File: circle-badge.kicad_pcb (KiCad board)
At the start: 2 copper layers, 100 x 140 mm, 41 parts, among them J3 USB_C_Receptacle_USB2.0_16P, J4 Qwiic, Q1 CJ2302, Q2 CJ2305, SW1 POWER, SW4 RESET, SW5 SELECT, U1 HX9193-33GB, U2 QX2304, U3 Wio-SX1262, U4 ESP32-C3-MINI-1, X1 #badgelife

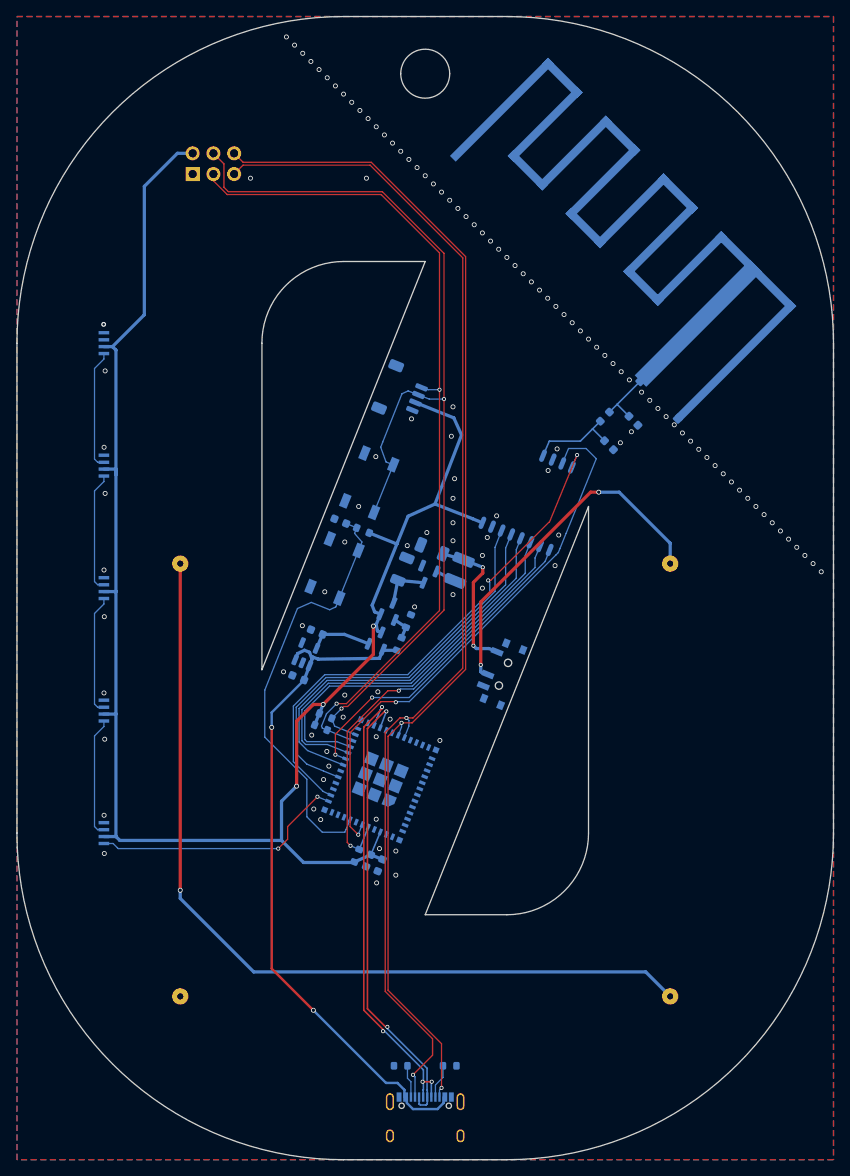
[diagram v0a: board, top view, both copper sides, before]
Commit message: Added front artwork and token on the back
Also:
- Tweaked the trace to the antenna to hopefully better match 50ohm impedance
- Tweaked all traces to use fillet on all corners
- Added/fixed parts information

Signed-off-by: Thomas Flummer <tf@flummer.net>
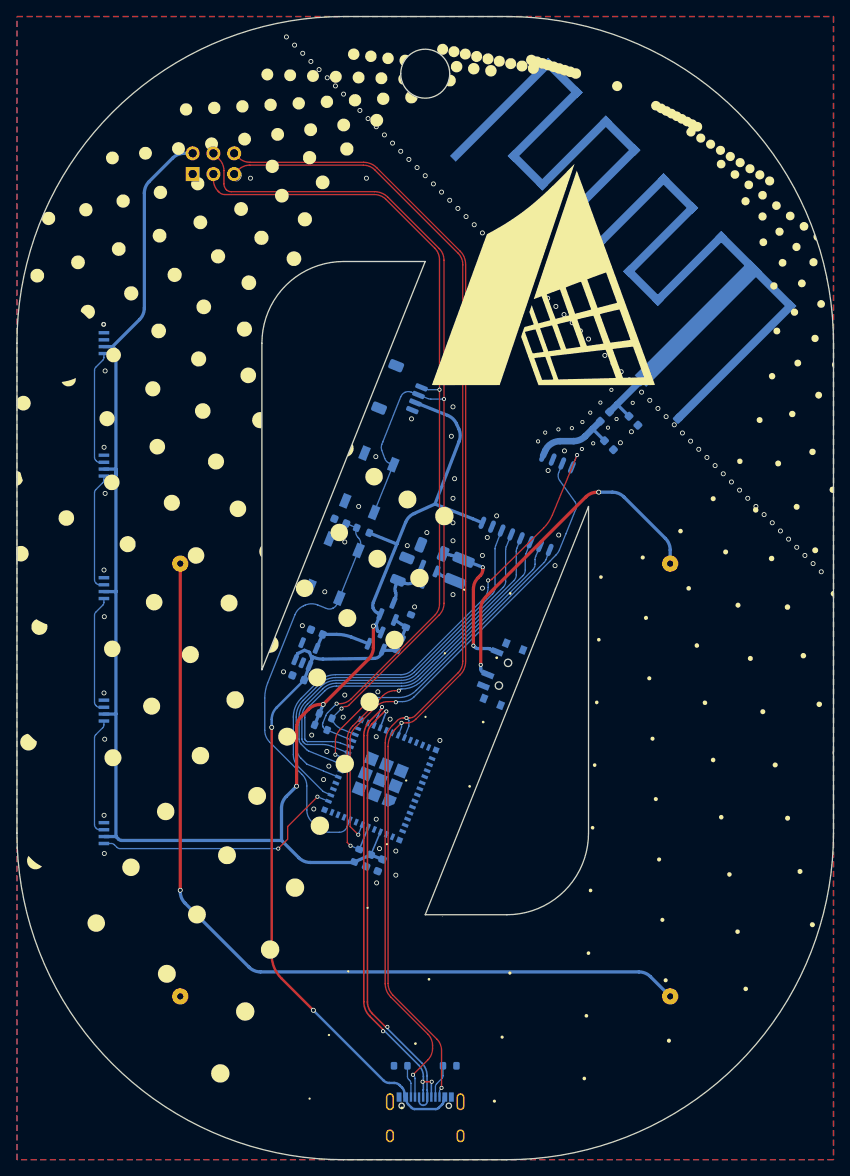
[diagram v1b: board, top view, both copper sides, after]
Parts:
- added G***: LOGO, LOGO, F.Cu at (104.8, 96.5)
- added G***: LOGO, LOGO, B.Cu at (75.2, 77.5)
- added G***: LOGO, LOGO, B.Cu at (67.0, 68.5)
- added G***: LOGO, LOGO, B.Cu at (100.0, 100.0)
- BT1, BT2: value Battery_Cell -> BH-AA-A1AJ020
- D1, D2, D3, D4, D5: value WS2812B-2020 -> WS2812B-4020
- J3: value USB_C_Receptacle_USB2.0_16P -> TYPE-C16PIN
- J4: value Qwiic -> 1.0T-4P
- SW1: value POWER -> MK-12C02-G015
- SW4: value RESET -> TS5220A
- SW5: value SELECT -> TS5220A
- U1: value HX9193-33GB -> XC6210B332MR
- U3: value Wio-SX1262 -> Wio-SX1262 / 113991436
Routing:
- net /LoRa SX1262/BUSY: track 67.3 -> 60.7 mm
- net VCC: track 214.9 -> 213.7 mm
- net /esp31-c3-mini/N_RST: track 52.7 -> 51.6 mm
- net /SAO_GPIO2: track 147.0 -> 146.0 mm
- net /SAO_GPIO1: track 145.6 -> 144.8 mm
- net /SDA: track 123.3 -> 122.5 mm
- net /LoRa SX1262/DIO1: track 65.4 -> 64.6 mm
- net /PSU 2xAA USB 3v3/USB_BUS_POWER: track 84.2 -> 83.5 mm
- net /LoRa SX1262/NSS: track 49.5 -> 49.0 mm
- net /esp31-c3-mini/USB_D+: track 56.4 -> 55.9 mm
- net GND: vias 122 -> 135
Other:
- board text added: "Design: Files: License: Rev:"
- board text added: "Sponsored by:"
- board text added: "hxr.social/@thomasflummer github.com/bornhack/badge2025 CC-BY-SA 1.1"
- board text removed: "Design: Files: License:"
- board text removed: "P R O T O T Y P E"
- board text removed: "hxr.social/@thomasflummer github.com/bornhack/badge2025 CC-BY-SA"
